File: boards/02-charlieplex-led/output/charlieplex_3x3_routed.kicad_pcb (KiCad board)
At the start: 2 copper layers, 50 x 55 mm, 14 parts, among them U1 MCU

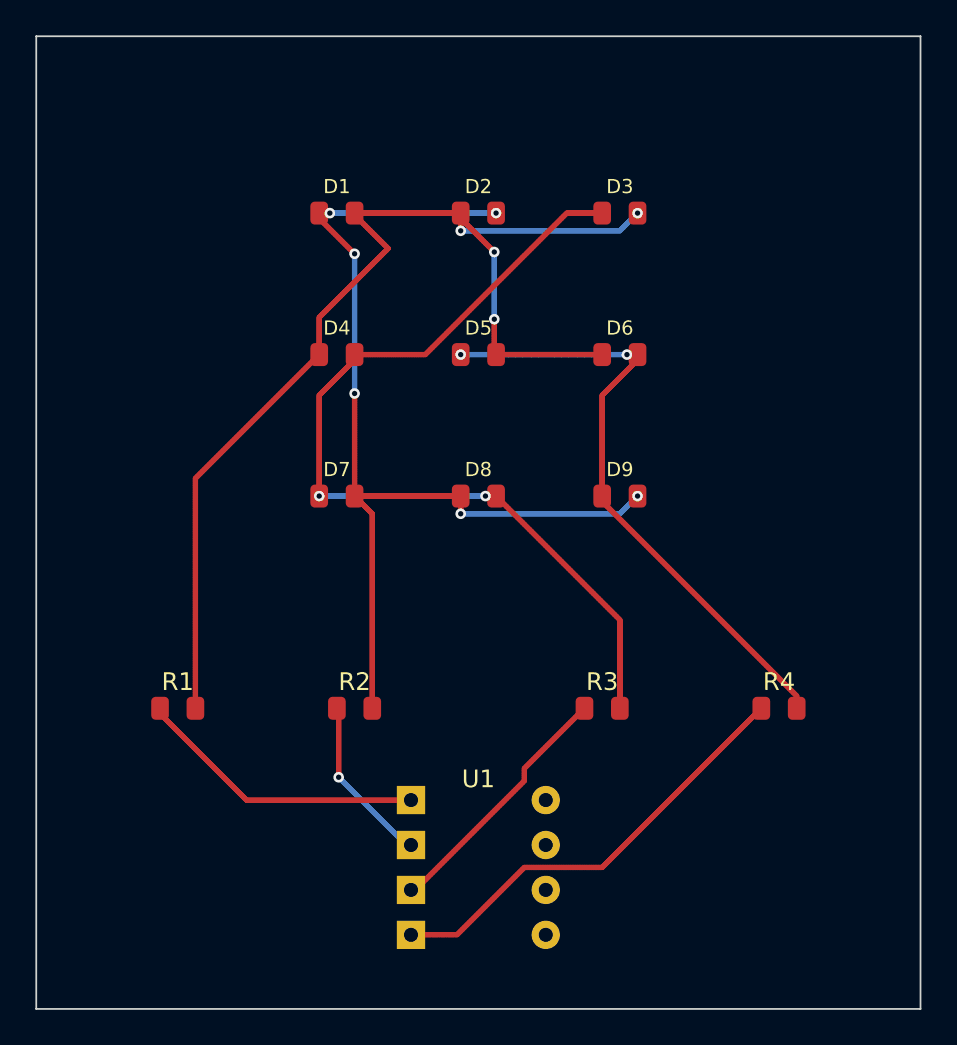
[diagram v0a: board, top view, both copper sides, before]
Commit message: fix(board): Increase LED footprint silkscreen text height to 1.0mm
Update charlieplex LED board to use 1.0mm text height for LED
footprints, matching the JLCPCB minimum recommendation. This resolves
9 DRC warnings that were flagged for text height below 1.0mm.

Changes:
- Update generate_pcb.py LED footprint text from 0.8mm to 1.0mm
- Increase text thickness from 0.12 to 0.15 for consistency
- Regenerate charlieplex_3x3.kicad_pcb with new font sizes
- Regenerate charlieplex_3x3_routed.kicad_pcb with new font sizes

Closes #859

Co-Authored-By: Claude Opus 4.5 <noreply@anthropic.com>
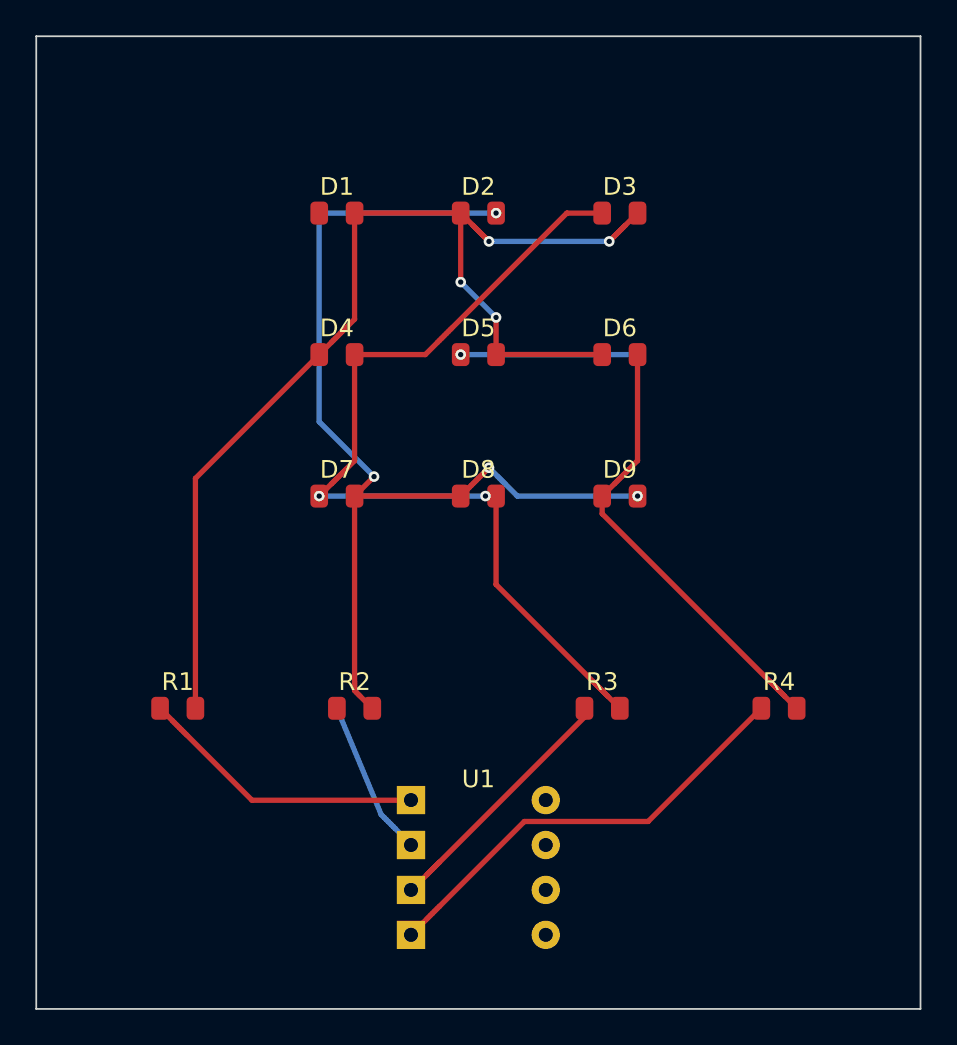
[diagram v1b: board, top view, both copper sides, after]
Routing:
- net NODE_A: track 65.5 -> 63.9 mm
- net NODE_B: track 56.7 -> 57.5 mm, vias 6 -> 4
- net LINE_B: track 9.65 -> 8.94 mm, vias 1 -> 0
- net NODE_D: vias 2 -> 1

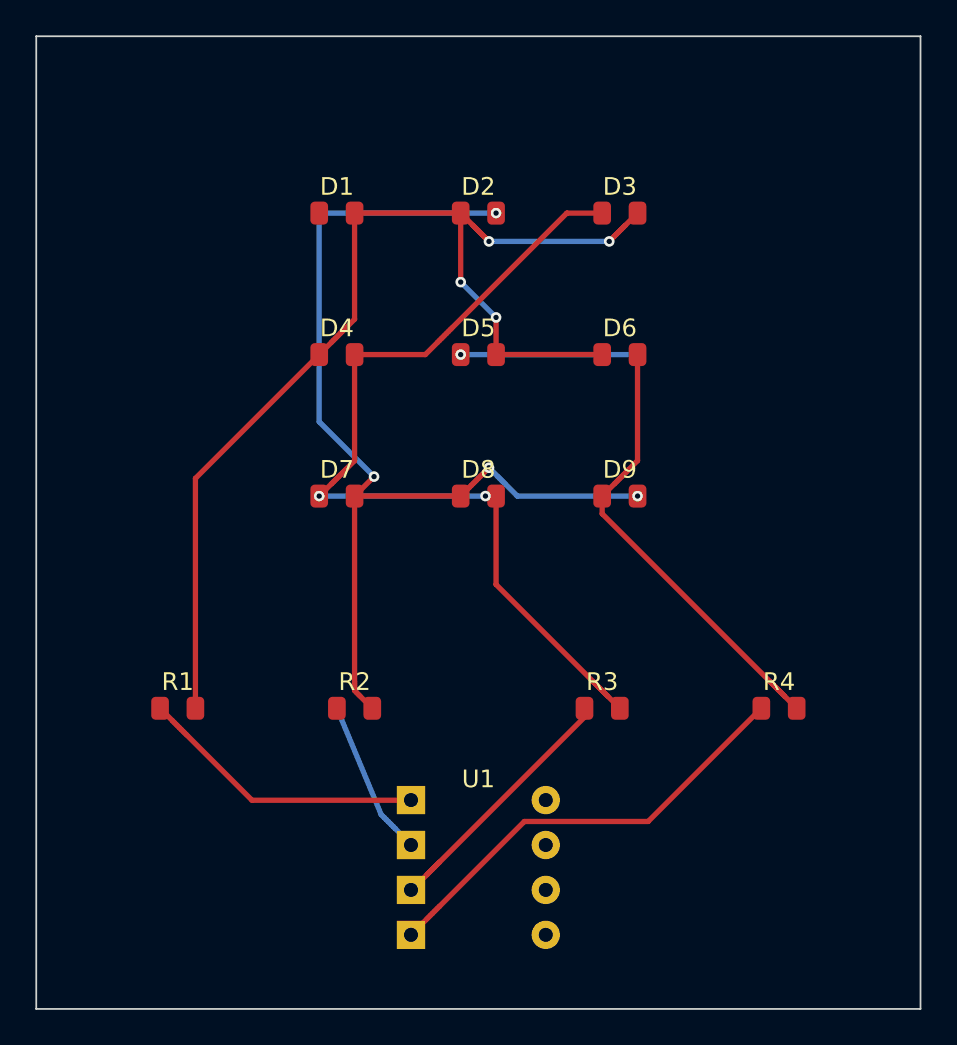
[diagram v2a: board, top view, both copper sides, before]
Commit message: fix(footprint): use R_0805 in default profile and fix board 02 U1 footprint (#1545)
Change the default footprint selector profile to map all resistor values
to R_0805_2012Metric instead of R_0402_1005Metric, matching what the PCB
generation scripts actually place. Also fix board 02's U1 schematic
footprint from PinHeader_1x08 to DIP-8_W7.62mm to match its PCB footprint.

Regenerate output files for boards 01 and 02 to reflect corrected footprints.

Co-authored-by: Claude Opus 4.6 <noreply@anthropic.com>
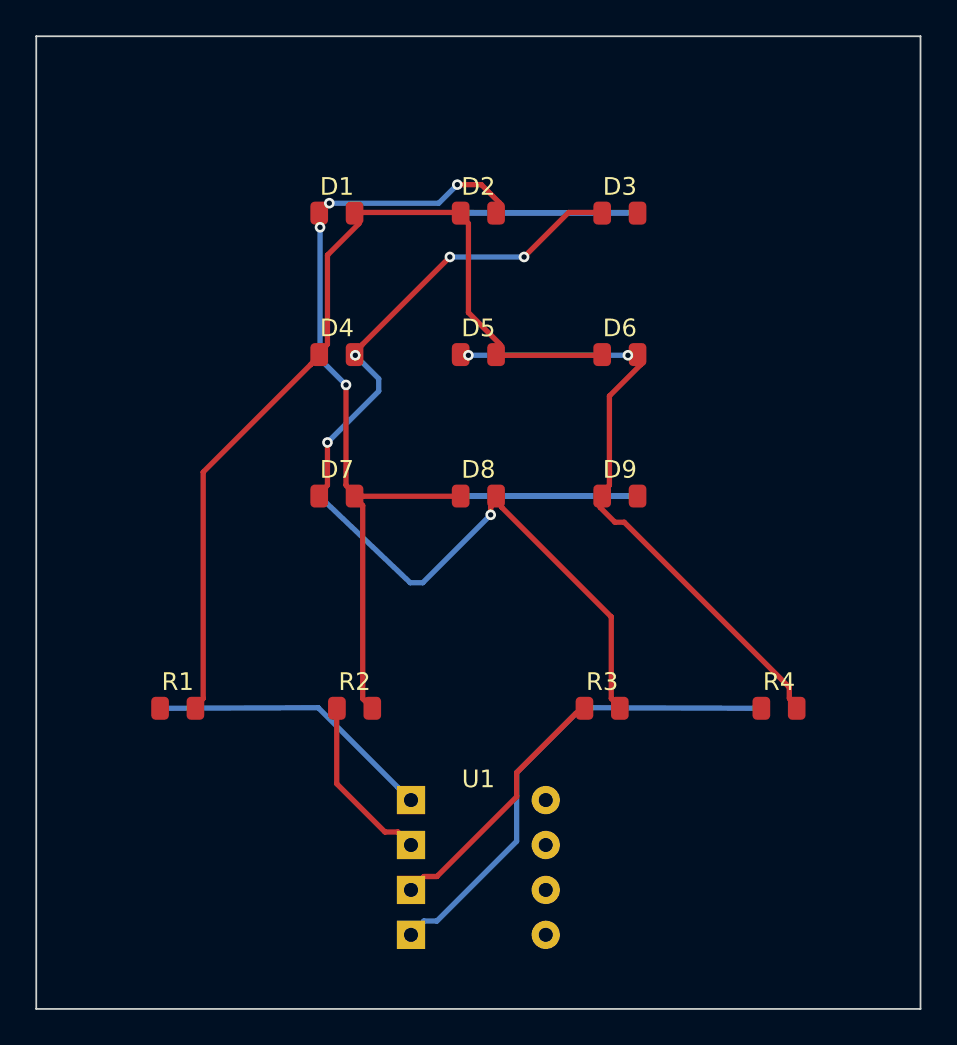
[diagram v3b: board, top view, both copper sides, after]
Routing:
- net NODE_B: track 57.5 -> 66.5 mm
- net NODE_A: track 63.9 -> 72.1 mm, vias 4 -> 0
- net NODE_C: track 51.0 -> 56.5 mm, vias 2 -> 5
- net LINE_D: track 25.1 -> 27.4 mm
- net LINE_B: track 8.94 -> 9.90 mm
- net NODE_D: track 35.4 -> 35.8 mm, vias 1 -> 2

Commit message: fix(boards): connect unused MCU pins to GND in boards 02 and 03
Unused MCU digital input pins were left without net assignments in the
PCB generators, producing pads with no net clause in the KiCad PCB
files. JLCPCB's automated review flags these unconnected pads and holds
orders for clarification. Connect all unused inputs to GND -- standard
practice that prevents floating inputs and eliminates review holds.

Board 02: pins 5, 6 (GND net 10)
Board 03: pins 5, 6, 18, 19, 20, 21, 22, 31 (GND net 3)

Co-Authored-By: Claude Opus 4.6 <noreply@anthropic.com>
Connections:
- U1 pad 5: (no net) -> GND
- U1 pad 6: (no net) -> GND
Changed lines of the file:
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@@
     (pad "3" thru_hole rect (at -3.810 1.270) (size 1.6 1.6) (drill 0.8) (layers "*.Cu" "*.Mask") (net 3 "LINE_C"))
     (pad "4" thru_hole rect (at -3.810 3.810) (size 1.6 1.6) (drill 0.8) (layers "*.Cu" "*.Mask") (net 4 "LINE_D"))
-    (pad "5" thru_hole oval (at 3.810 3.810) (size 1.6 1.6) (drill 0.8) (layers "*.Cu" "*.Mask") )
-    (pad "6" thru_hole oval (at 3.810 1.270) (size 1.6 1.6) (drill 0.8) (layers "*.Cu" "*.Mask") )
+    (pad "5" thru_hole oval (at 3.810 3.810) (size 1.6 1.6) (drill 0.8) (layers "*.Cu" "*.Mask") (net 10 "GND"))
+    (pad "6" thru_hole oval (at 3.810 1.270) (size 1.6 1.6) (drill 0.8) (layers "*.Cu" "*.Mask") (net 10 "GND"))
     (pad "7" thru_hole oval (at 3.810 -1.270) (size 1.6 1.6) (drill 0.8) (layers "*.Cu" "*.Mask") (net 9 "VCC"))
     (pad "8" thru_hole oval (at 3.810 -3.810) (size 1.6 1.6) (drill 0.8) (layers "*.Cu" "*.Mask") (net 10 "GND"))
